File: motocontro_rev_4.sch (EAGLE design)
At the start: 18 parts

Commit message: Thurs Morning Buck converter + clean
Added a part for the stingray buck converter. Must figure out how to actually connect the pins and build a separate docking board. Also cleaned up the schematic a little bit
Much left to do
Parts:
- added U$3: GE_STINGRAY_H, motocontro_rev_4:GE_STINGRAY_H
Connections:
- removed net #LIN: U$1.1_LIN
- removed net HIN: U$1.3_HIN
- new net PWM: U$1.1_LIN, U$1.3_HIN
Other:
- note added: "BUCK Converter"
- note added: "Half-Bridge Circuit"
- note added: "Made this part for the Stingray We actually stilll need to make a breakout board that docks for this BUCK"
- note added: "Must make a Schottky diode part Check BOM"
- note added: "Need: PWM pins #SD pin."
- note added: "Teensy"
- note removed: "Need: PWM pins, OPAMP pin, OPAMP filter, #SD pin."
- moved on the sheet: BATTERY, CDT, CSD, CURR_RES, CURR_RES1, HS_FET, LS_FET, MOTOR, R3, R4, RDT, RSD

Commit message: SCH almost done.
Adds diode
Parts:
- added C1, C3: 22u, adafruit:CPOL-US175TMP-0810
- added C2: 100 u, adafruit:C-US225-113X268
- added R5, R6, R7: (no value), adafruit:R-US_R0805
- added U$4: TRACO-TSR-1-2450, r-78xx_10:TRACO-TSR-1-2450
- added U$5: FERD40H100SG-TR, motocontro_rev_4:FERD40H100SG-TR
- R1, R2, RDT, RSD: device eagle-ltspice:RR2012 -> adafruit:R-US_R0805
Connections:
- net V_BOOT renamed VBOOT
- removed net N$1: U$2.GND3
- removed net N$4: BATTERY.+, HS_FET.D, MOTOR.P$1
- new net 5V: U$2.VIN, U$4.OUT
- new net GND: C2.2, U$3.VI-
- new net OP+: R5.1, R6.1, R7.2, U$1.9_OP+
- new net VBUS: BATTERY.+, C2.1, HS_FET.D, MOTOR.P$1, U$3.VI+, U$5.C
- net DGND: now also C1.-, C3.-, R7.1, U$2.GND3, U$3.VO-, U$4.GND
- net OUT: now also U$5.A
- net RSENSE+: now also R5.2; no longer U$1.9_OP+
- net VCC: now also C1.+, C3.+, R6.2, U$3.VO+, U$4.IN
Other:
- note added: "DeadTime"
- note added: "Driver"
- note added: "Fault Disable Time"
- note added: "MCU"
- note added: "OpAmp Support"
- note added: "Power"
- note removed: "BUCK Converter"
- note removed: "Need: PWM pins #SD pin."
- note removed: "Teensy"
- moved on the sheet: BATTERY, CBOOT, CDT, CDT1, CSD, CURR_RES, CURR_RES1, HS_FET, LS_FET, MOTOR, R3, R4

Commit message: Finished schematic, board almost done
Board layout in progress
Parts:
- removed CURR_RES: 40 mOhm, eagle-ltspice:RR6332
- added RSENSE1: 37m, motocontro_rev_4:RESSENSE_2818
- CURR_RES1: value 40 mOhm -> 37m; device eagle-ltspice:RR6332 -> motocontro_rev_4:RESSENSE_2818
- renumbered U$4 to LDO, U$5 to SCHOTTKY
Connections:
- removed net #SD/OD: CSD.2, RSD.1, U$1.2_SD/OD
- new net SD/OD: CSD.2, RSD.1, U$1.2_SD/OD, U$2.5
- net GND: now also U$3.ON/OFF
- net OPOUT: now also U$2.14/A0
- net PGND: now also RSENSE1.1; no longer CURR_RES.1
- net PWM: now also U$2.6
- net RSENSE+: now also RSENSE1.2; no longer CURR_RES.2
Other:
- note added: "I think this should be connected to DGND?"
- note added: "PGND is used for the power ground. DGND is used for the digital logic They will connect through GND trace"
- note removed: "Get Rsense package from previous REV"
- note removed: "PGND is used for the power ground. DGND is used for the digital logic"

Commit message: redos some layout
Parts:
- C1: value 22u -> 1u; device adafruit:CPOL-US175TMP-0810 -> Nordic_nRF:CAPACITOR_0805_M
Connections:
- net DGND: now also C1.2; no longer C1.-
- net VCC: now also C1.1; no longer C1.+

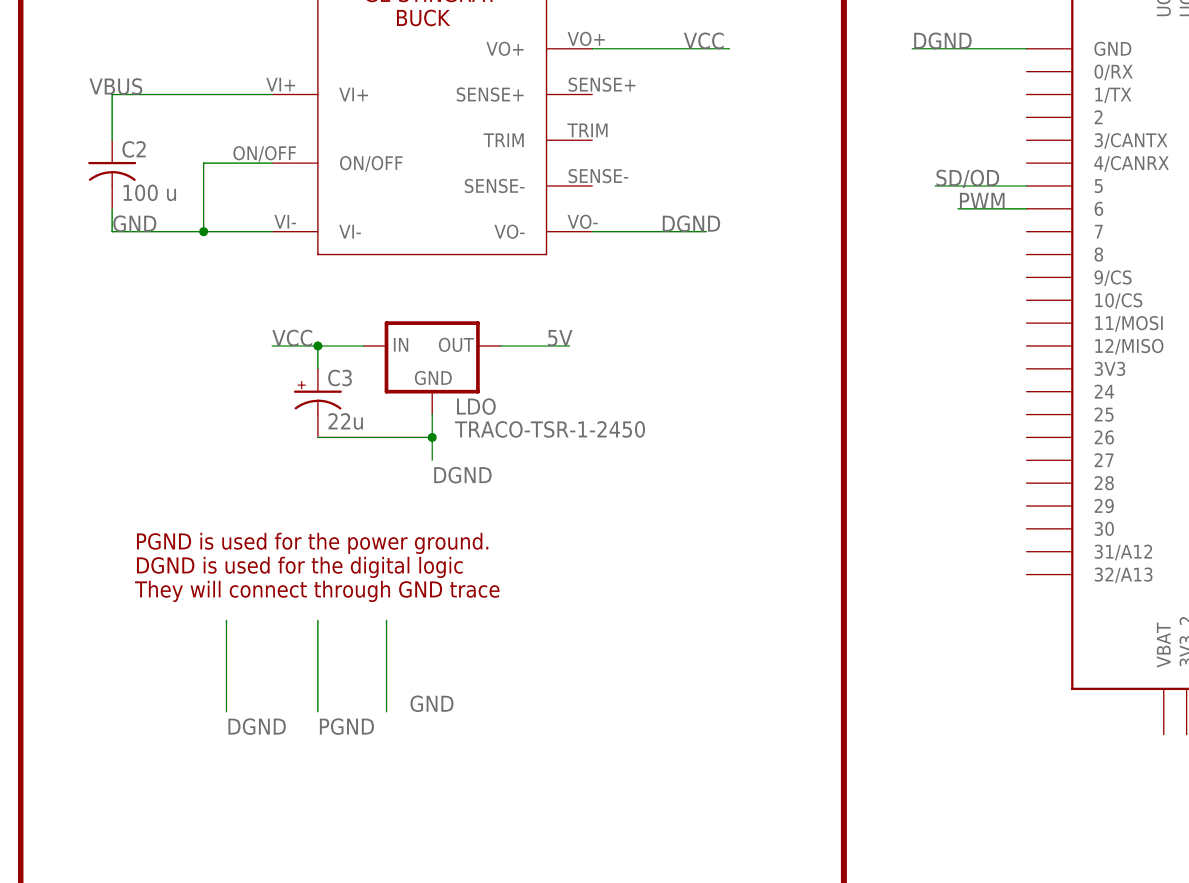
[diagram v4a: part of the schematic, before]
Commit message: finishes layout
finishes layout and minimal changes to teensy pinout.
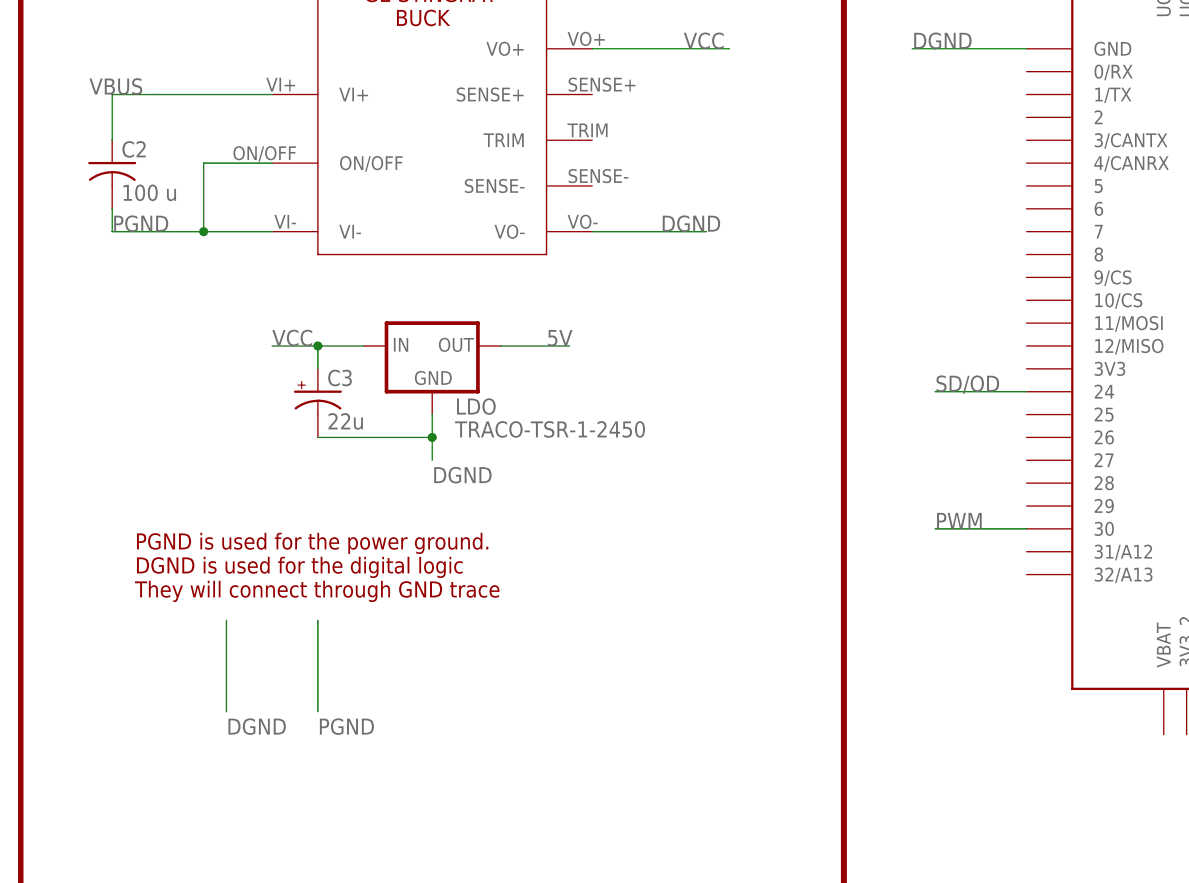
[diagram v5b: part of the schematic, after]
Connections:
- removed net GND: C2.2, U$3.ON/OFF, U$3.VI-
- net PGND: now also C2.2, U$3.ON/OFF, U$3.VI-
- net PWM: now also U$2.30; no longer U$2.6
- net SD/OD: now also U$2.24; no longer U$2.5

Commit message: Design Review
Added a ton of notes of things to be updated
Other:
- note added: "Add LEDs to power regulators"
- note added: "Add heatsink to FET package"
- note added: "Add test pads. Add headers for GND Add a U-shape"
- note added: "Connect with a 0Ohm jumper, or jumper."
- note added: "Make an SPI bus to run to an OLED display in the front"
- note added: "Make possible to drive with two signals."
- note added: "Make this tunable. Pot, triple parallel or something"
- note added: "Should be PGND"
- note added: "Stingray is overkill. Look for 10-1W buck"
- note added: "add a connector for a 15V fan"
- note added: "connect a couple of GPIO or input headers hanging off"
- note added: "consider adding two in parallel"
- note added: "put some LEDs as GPIOs to the teensy"
- note removed: "I think this should be connected to DGND?"
- note removed: "Must make a Schottky diode part Check BOM"
- moved on the sheet: BATTERY, CURR_RES1, HS_FET, LS_FET, MOTOR, R3, R4, RSENSE1, SCHOTTKY

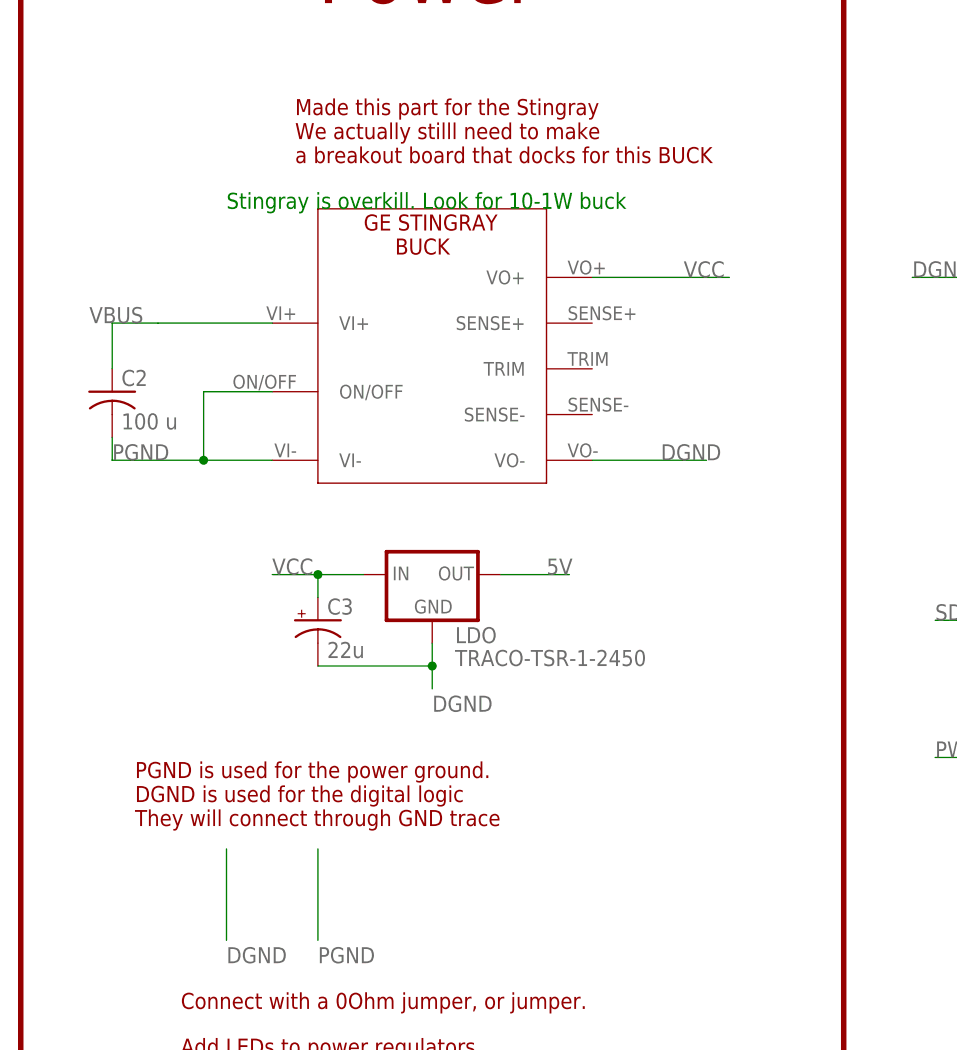
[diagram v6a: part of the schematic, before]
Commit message: added ground connections
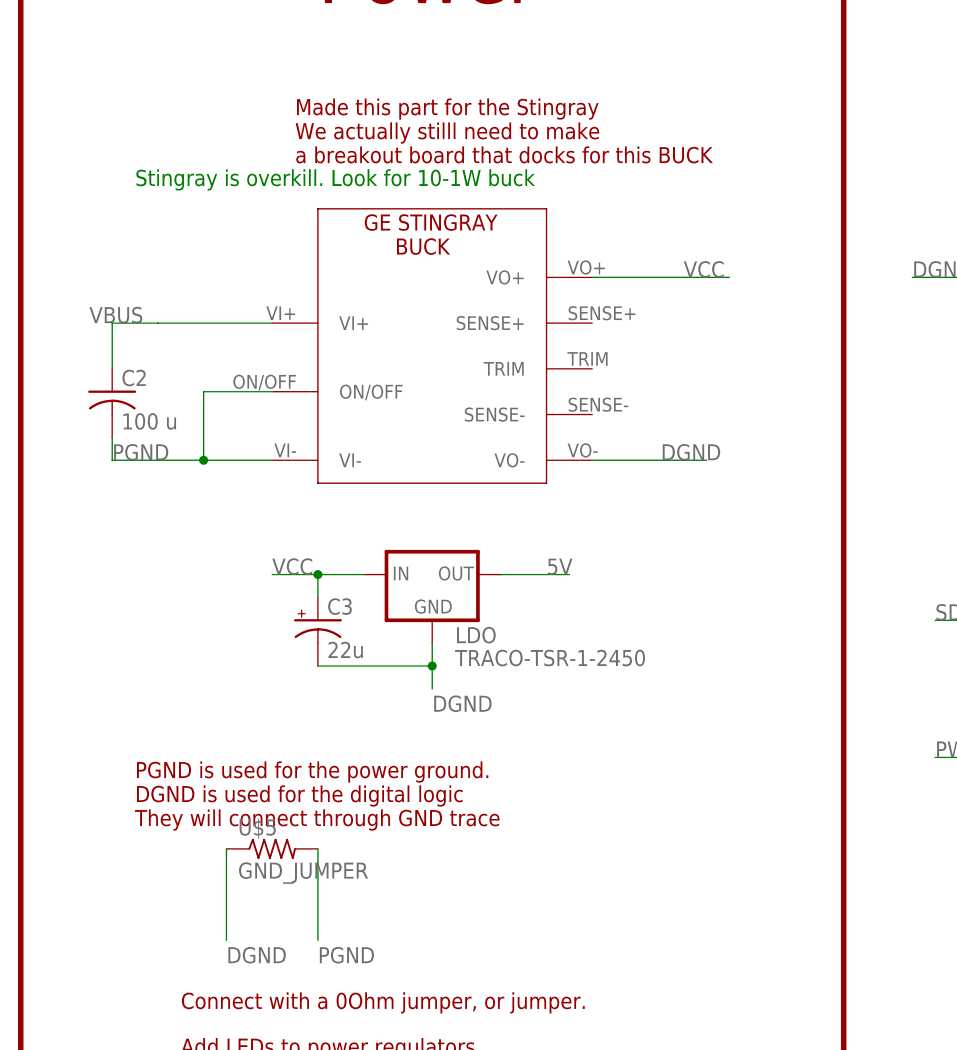
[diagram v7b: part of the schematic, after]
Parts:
- added U$5: GND_JUMPER, motocontro_rev_4:GND_JUMPER
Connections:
- net DGND: now also U$5.1
- net PGND: now also U$5.2
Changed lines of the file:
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@@
 <part name="SCHOTTKY" library="motocontro_rev_4" deviceset="FERD40H100SG-TR" device="" package3d_urn="urn:adsk.eagle:package:38457/1"/>
 <part name="RSENSE1" library="motocontro_rev_4" deviceset="RESSENSE_2818" device="" package3d_urn="urn:adsk.eagle:package:2273943/1" value="37m"/>
+<part name="U$5" library="motocontro_rev_4" deviceset="GND_JUMPER" device=""/>
 </parts>
 <sheets>
@@
 <text x="-45.72" y="-66.04" size="2.1844" layer="94">Fault Disable Time</text>
 <text x="40.64" y="-45.72" size="1.778" layer="94">Should be PGND </text>
-<text x="-203.2" y="30.48" size="1.778" layer="91">Stingray is overkill. Look for 10-1W buck</text>
+<text x="-213.36" y="33.02" size="1.778" layer="91">Stingray is overkill. Look for 10-1W buck</text>
 <text x="-208.28" y="-58.42" size="1.778" layer="94">Connect with a 0Ohm jumper, or jumper.</text>
 <text x="40.64" y="-25.4" size="1.778" layer="94">Make this tunable.
@@
 <attribute name="VALUE" x="168.402" y="-67.31" size="1.778" layer="96" rot="R90"/>
 </instance>
+<instance part="U$5" gate="G$1" x="-198.12" y="-40.64">
+<attribute name="NAME" x="-201.93" y="-39.1414" size="1.778" layer="95"/>
+<attribute name="VALUE" x="-201.93" y="-43.942" size="1.778" layer="96"/>
+</instance>
 </instances>
 <busses>
@@
 <wire x1="-193.04" y1="-40.64" x2="-193.04" y2="-50.8" width="0.1524" layer="91"/>
 <label x="-193.04" y="-53.34" size="1.778" layer="95"/>
+<pinref part="U$5" gate="G$1" pin="2"/>
 </segment>
 <segment>
@@
 <wire x1="-203.2" y1="-40.64" x2="-203.2" y2="-50.8" width="0.1524" layer="91"/>
 <label x="-203.2" y="-53.34" size="1.778" layer="95"/>
-</segment>
-</net>
+<pinref part="U$5" gate="G$1" pin="1"/>
+</segment>
+</net>
